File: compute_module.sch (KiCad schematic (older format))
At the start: 24 parts, among them Q1 2N7002P.215

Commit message: Added datasheet links to BOM
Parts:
- MD1: Manf _ -> (none); Manf# _ -> (none); Optn _ -> (none)
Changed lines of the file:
@@
 F 1 "Board_RPi_CM3_200pConnector_multipart" H 2300 7600 50  0000 C CNN
 F 2 "Conn_TE-DDR2-SODIMM:Conn_TE-DDR2-SODIMM-0.6-200P-doublesided" H 8275 1300 10  0001 C CNN
-F 3 "_" H 8275 1300 10  0001 C CNN
-F 4 "_" H 8275 1300 10  0001 C CNN "Manf#"
-F 5 "_" H 8275 1300 10  0001 C CNN "Manf"
-F 6 "_" H 8275 1300 10  0001 C CNN "Optn"
+F 3 "https://www.tme.eu/en/Document/4b83792fd18cac93e642ba1f5319bf1c/1473005-4.pdf" H 8275 1300 10  0001 C CNN
 	1    2300 4150
 	1    0    0    -1
@@
 F 1 "Board_RPi_CM3_200pConnector_multipart" H 10300 3650 50  0000 C CNN
 F 2 "Conn_TE-DDR2-SODIMM:Conn_TE-DDR2-SODIMM-0.6-200P-doublesided" H 16275 500 10  0001 C CNN
-F 3 "_" H 16275 500 10  0001 C CNN
-F 4 "_" H 16275 500 10  0001 C CNN "Manf#"
-F 5 "_" H 16275 500 10  0001 C CNN "Manf"
-F 6 "_" H 16275 500 10  0001 C CNN "Optn"
+F 3 "https://www.tme.eu/en/Document/4b83792fd18cac93e642ba1f5319bf1c/1473005-4.pdf" H 16275 500 10  0001 C CNN
 	2    10300 3350
 	-1   0    0    -1
@@
 F 1 "Board_RPi_CM3_200pConnector_multipart" H 10350 6500 50  0000 C CNN
 F 2 "Conn_TE-DDR2-SODIMM:Conn_TE-DDR2-SODIMM-0.6-200P-doublesided" H 16325 2300 10  0001 C CNN
-F 3 "_" H 16325 2300 10  0001 C CNN
-F 4 "_" H 16325 2300 10  0001 C CNN "Manf#"
-F 5 "_" H 16325 2300 10  0001 C CNN "Manf"
-F 6 "_" H 16325 2300 10  0001 C CNN "Optn"
+F 3 "https://www.tme.eu/en/Document/4b83792fd18cac93e642ba1f5319bf1c/1473005-4.pdf" H 16325 2300 10  0001 C CNN
 	3    10350 5150
 	-1   0    0    -1
@@
 F 1 "Board_RPi_CM3_200pConnector_multipart" H 5550 3000 50  0000 C CNN
 F 2 "Conn_TE-DDR2-SODIMM:Conn_TE-DDR2-SODIMM-0.6-200P-doublesided" H 11475 -1050 10  0001 C CNN
-F 3 "_" H 11475 -1050 10  0001 C CNN
-F 4 "_" H 11475 -1050 10  0001 C CNN "Manf#"
-F 5 "_" H 11475 -1050 10  0001 C CNN "Manf"
-F 6 "_" H 11475 -1050 10  0001 C CNN "Optn"
+F 3 "https://www.tme.eu/en/Document/4b83792fd18cac93e642ba1f5319bf1c/1473005-4.pdf" H 11475 -1050 10  0001 C CNN
 	4    5500 1800
 	1    0    0    -1
@@
 F 1 "Board_RPi_CM3_200pConnector_multipart" H 8300 2400 50  0000 C CNN
 F 2 "Conn_TE-DDR2-SODIMM:Conn_TE-DDR2-SODIMM-0.6-200P-doublesided" H 14275 -1350 10  0001 C CNN
-F 3 "_" H 14275 -1350 10  0001 C CNN
-F 4 "_" H 14275 -1350 10  0001 C CNN "Manf#"
-F 5 "_" H 14275 -1350 10  0001 C CNN "Manf"
-F 6 "_" H 14275 -1350 10  0001 C CNN "Optn"
+F 3 "https://www.tme.eu/en/Document/4b83792fd18cac93e642ba1f5319bf1c/1473005-4.pdf" H 14275 -1350 10  0001 C CNN
 	5    8300 1500
 	1    0    0    -1
@@
 F 1 "Board_RPi_CM3_200pConnector_multipart" H 10350 3000 50  0000 C CNN
 F 2 "Conn_TE-DDR2-SODIMM:Conn_TE-DDR2-SODIMM-0.6-200P-doublesided" H 16275 -1050 10  0001 C CNN
-F 3 "_" H 16275 -1050 10  0001 C CNN
-F 4 "_" H 16275 -1050 10  0001 C CNN "Manf#"
-F 5 "_" H 16275 -1050 10  0001 C CNN "Manf"
-F 6 "_" H 16275 -1050 10  0001 C CNN "Optn"
+F 3 "https://www.tme.eu/en/Document/4b83792fd18cac93e642ba1f5319bf1c/1473005-4.pdf" H 16275 -1050 10  0001 C CNN
 	7    10300 1800
 	-1   0    0    -1
@@
 F 1 "2N7002P.215" V 4250 1800 50  0000 L CNN
 F 2 "TO_SOT_Packages_SMD:SOT-23" H 4200 2150 50  0001 C CNN
-F 3 "" H 4000 2050 50  0000 C CNN
+F 3 "https://www.tme.eu/en/Document/fda24b70d66290936384ff869f03745e/2N7002P.pdf" H 4000 2050 50  0001 C CNN
 	1    4000 2050
 	1    0    0    -1
@@
 F 1 "Board_RPi_CM3_200pConnector_multipart" H 5250 6300 50  0000 C CNN
 F 2 "Conn_TE-DDR2-SODIMM:Conn_TE-DDR2-SODIMM-0.6-200P-doublesided" H 11175 1650 10  0001 C CNN
-F 3 "_" H 11175 1650 10  0001 C CNN
-F 4 "_" H 11175 1650 10  0001 C CNN "Manf#"
-F 5 "_" H 11175 1650 10  0001 C CNN "Manf"
-F 6 "_" H 11175 1650 10  0001 C CNN "Optn"
+F 3 "https://www.tme.eu/en/Document/4b83792fd18cac93e642ba1f5319bf1c/1473005-4.pdf" H 11175 1650 10  0001 C CNN
 	6    5200 4500
 	0    -1   -1   0

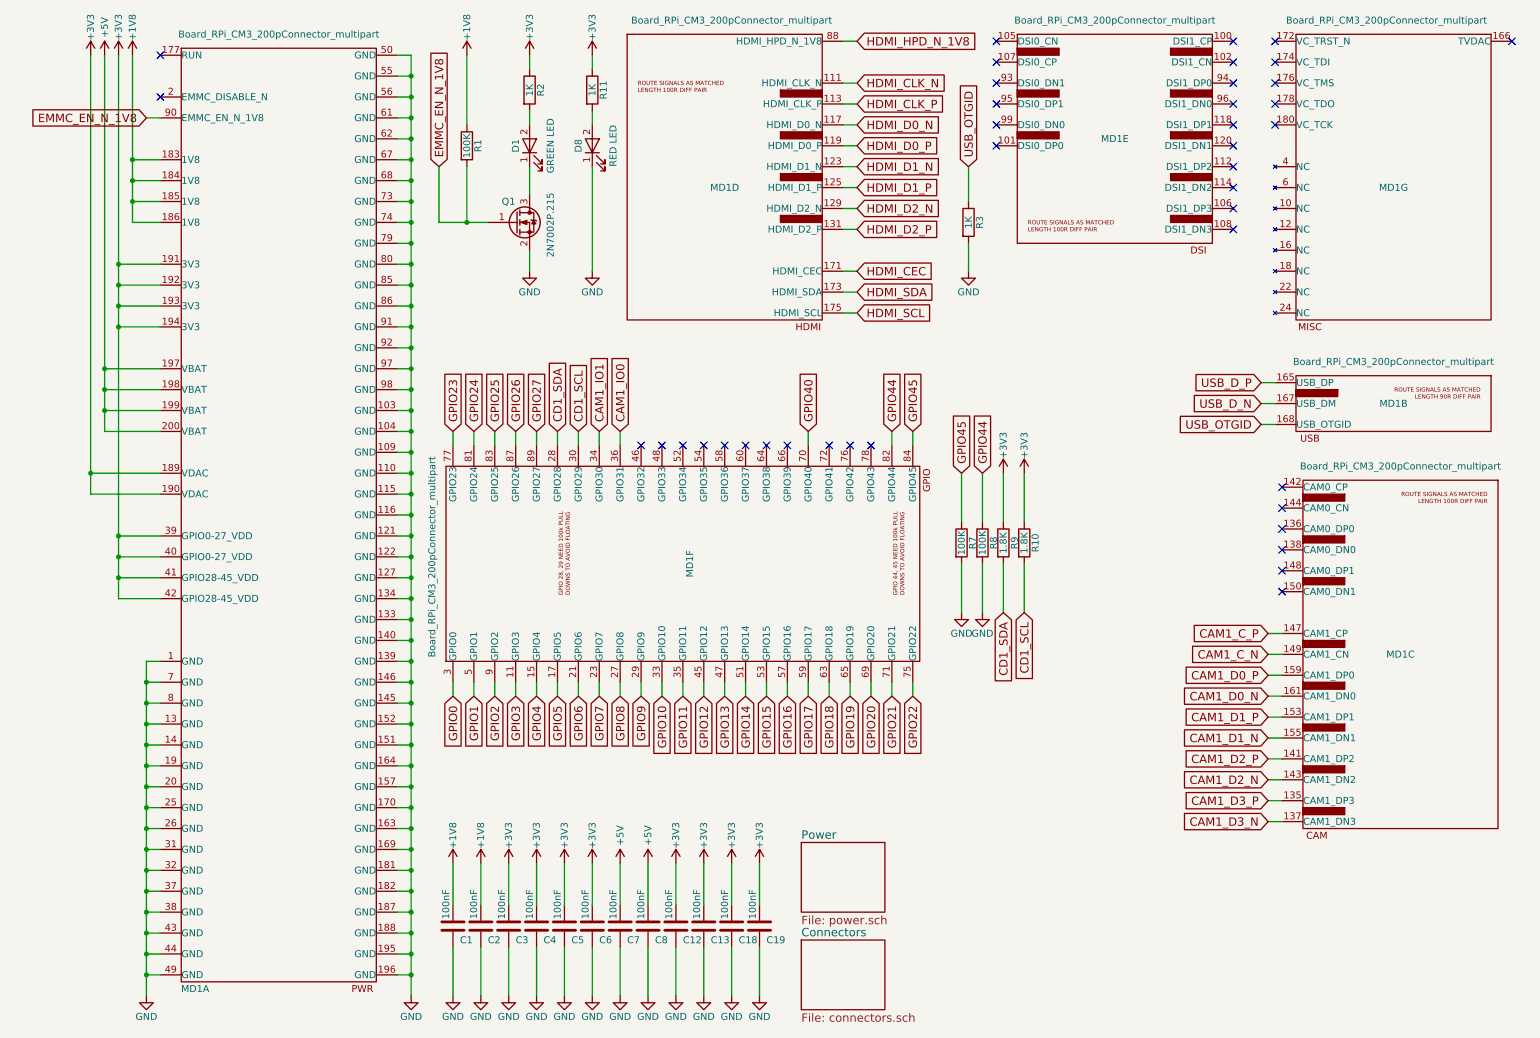
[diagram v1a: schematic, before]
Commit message: Schematic changes to support CAM0
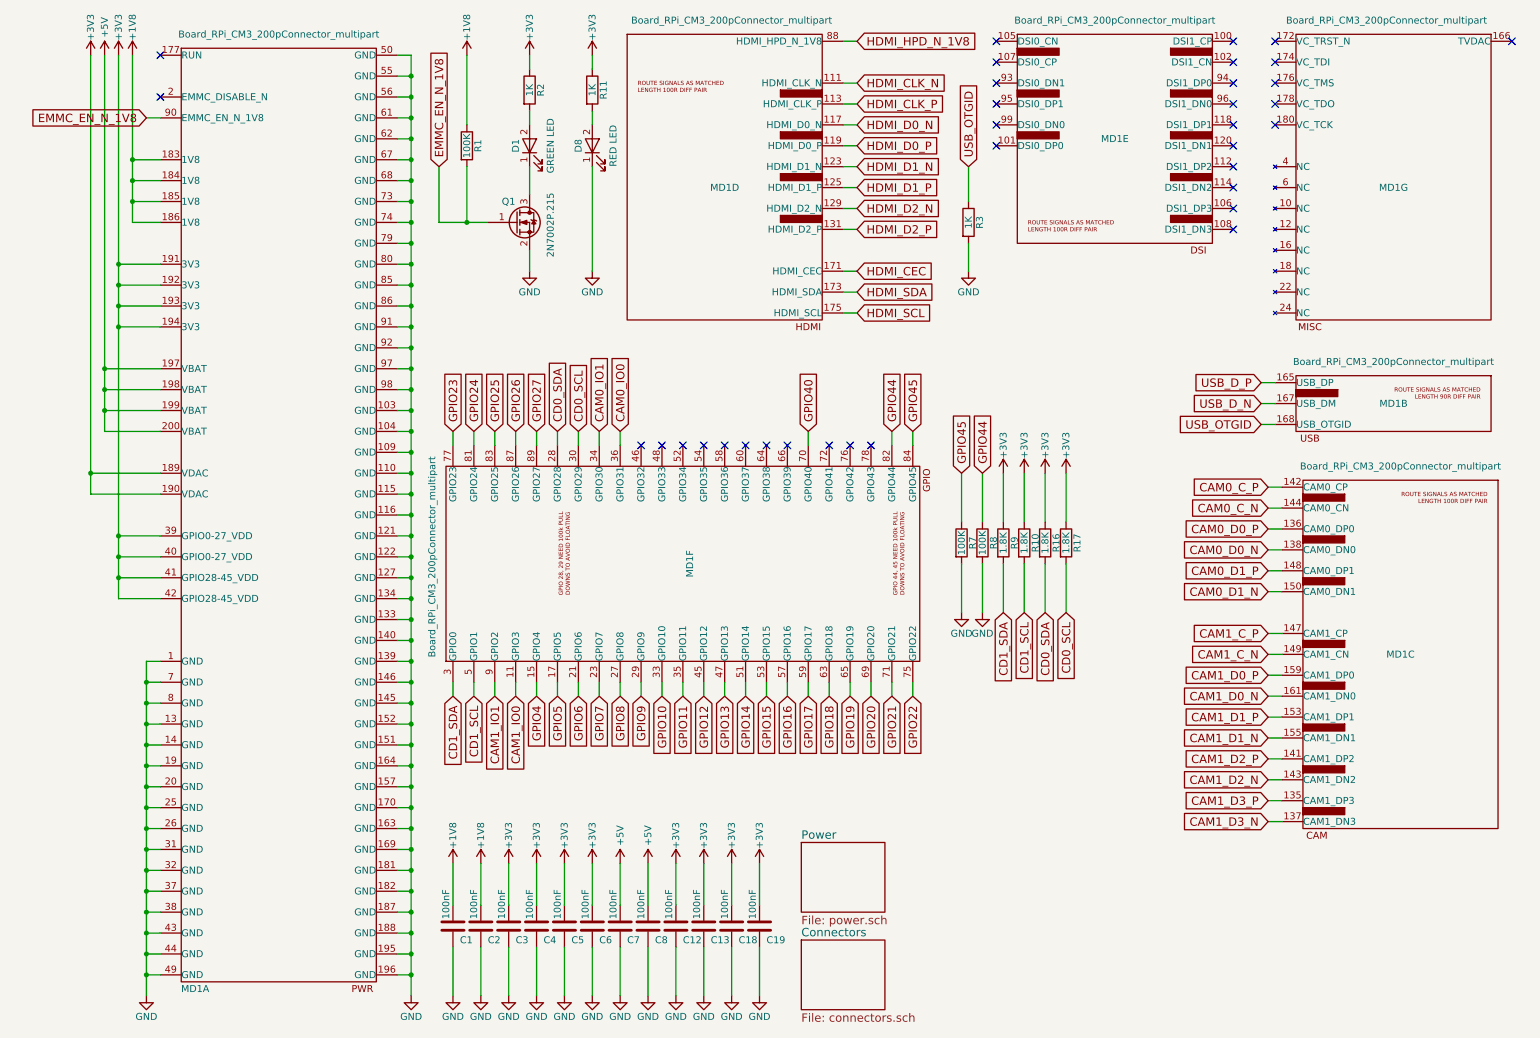
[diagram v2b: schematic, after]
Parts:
- added R16, R17: 1.8K, Resistors_SMD:R_0603_HandSoldering, symbol R
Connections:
- net GPIO0 is gone; now on net CD1_SDA: MD1.3 (GPIO0)
- net GPIO1 is gone; now on net CD1_SCL: MD1.5 (GPIO1)
- net GPIO2 is gone; now on net CAM1_IO1: MD1.9 (GPIO2)
- net GPIO3 is gone; now on net CAM1_IO0: MD1.11 (GPIO3)
- net +3V3: now also R16.1, R17.1
- net CAM1_IO0: no longer MD1.36 (GPIO31)
- net CAM1_IO1: no longer MD1.34 (GPIO30)
- net CD1_SCL: no longer MD1.30 (GPIO29)
- net CD1_SDA: no longer MD1.28 (GPIO28)
- net CAM0_D0_P: now reaches MD1.136 (CAM0_DP0)
- net CAM0_D0_N: now reaches MD1.138 (CAM0_DN0)
- net CAM0_C_P: now reaches MD1.142 (CAM0_CP)
- net CAM0_C_N: now reaches MD1.144 (CAM0_CN)
- net CAM0_D1_P: now reaches MD1.148 (CAM0_DP1)
- net CAM0_D1_N: now reaches MD1.150 (CAM0_DN1)
- new net CAM0_IO0: MD1.36 (GPIO31)
- new net CAM0_IO1: MD1.34 (GPIO30)
- new net CD0_SCL: MD1.30 (GPIO29), R17.2
- new net CD0_SDA: MD1.28 (GPIO28), R16.2
- no-connect marks 41 -> 35

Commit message: Initial PCB changes to support CAM0+CAM1
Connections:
- net CD0_SCL: now also R10.2; no longer R17.2
- net CD0_SDA: now also R9.2; no longer R16.2
- net CD1_SCL: now also R17.2; no longer R10.2
- net CD1_SDA: now also R16.2; no longer R9.2
